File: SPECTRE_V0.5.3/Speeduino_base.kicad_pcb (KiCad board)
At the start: 2 copper layers, 100 x 93 mm, 197 parts, among them J1 Conn_01x06_Male, J2 Conn_02x04_Odd_Even, J3 ProtoArea, Q1 AO3400, Q10 BSP78, Q11 BSP78, Q12 AO3400, Q13 BSP78, Q14 BSP78, Q15 BSP78, Q16 BSP78, Q17 BSP78, Q18 BSP78, Q19 BSP78, Q20 BSP78, Q21 BSP78, Q6 AO3400, Q7 AO3400, U1 MAX9926UAEE+, U10 MIC4427, U2 LM78M05_TO220, U3 TL431DBZ, U4 molex_48pin, U5 TJA1050, U6 MAX3232, U7 MIC4427, U8 MIC4427, U9 MIC4427

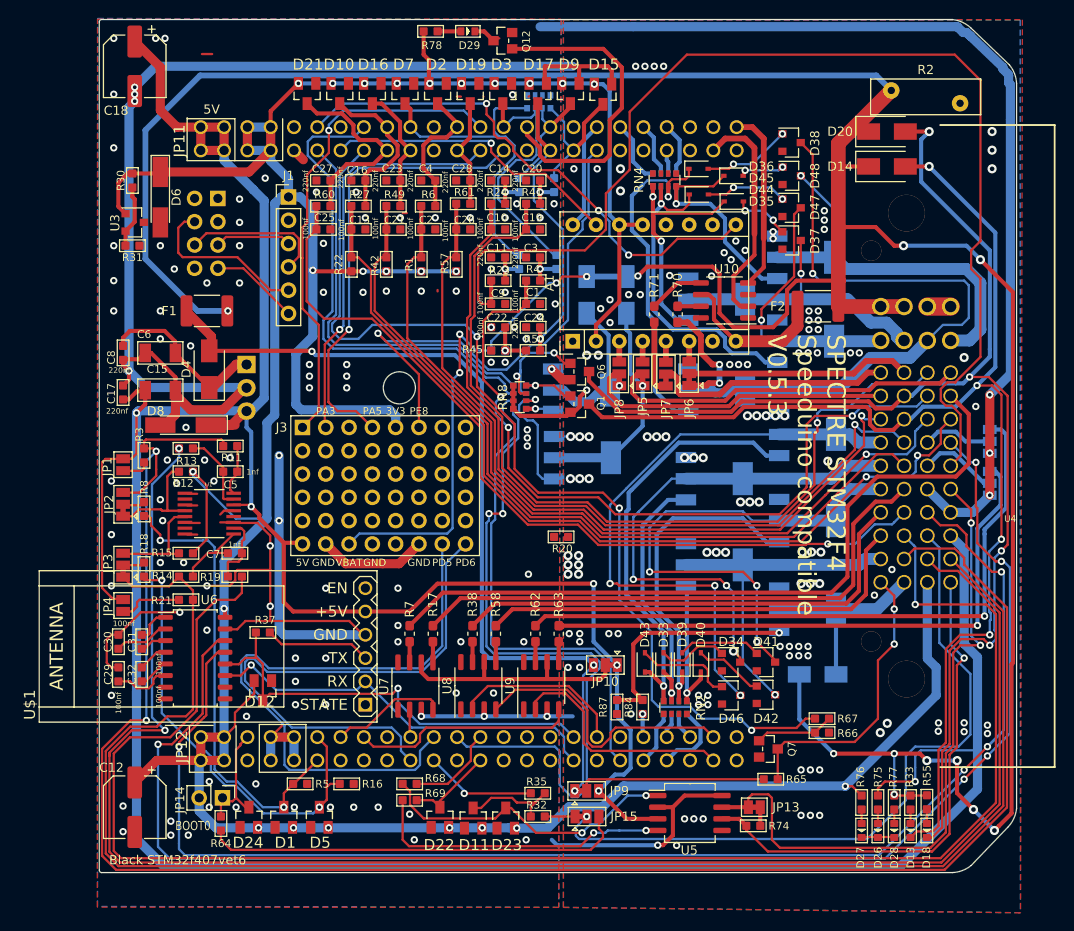
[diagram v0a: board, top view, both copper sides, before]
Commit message: Increased VBAT width
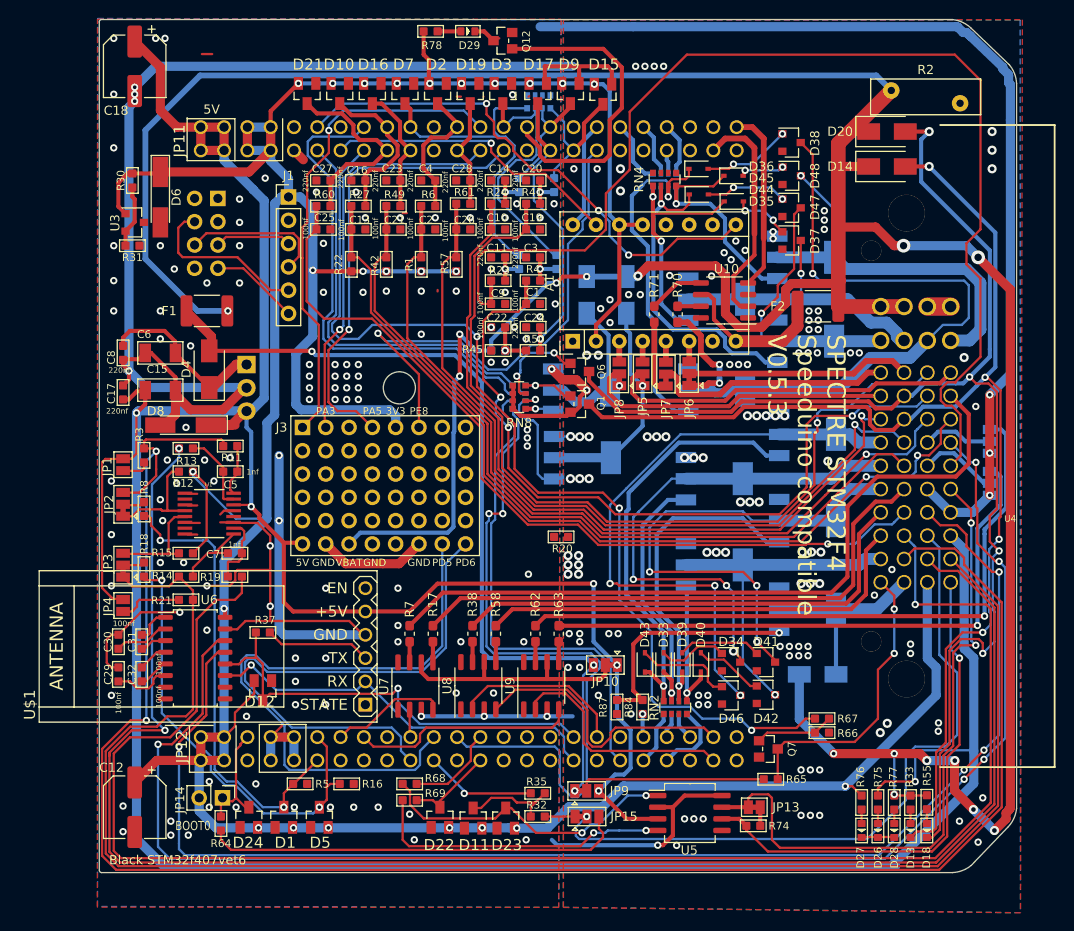
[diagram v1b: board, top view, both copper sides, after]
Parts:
- U4: footprint rusefi_lib:Molex_48 -> Speeduino_base:Molex_48
- moved RN4 0.07 mm to (165.2, 53.0)
- moved RN7 0.06 mm to (149.4, 76.7)
- moved RN8 0.06 mm to (149.4, 76.7)
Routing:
- net RS232_RX: track 150.8 -> 148.4 mm
- net PWR_GND: track 160.8 -> 163.0 mm, vias 129 -> 131
- net Net-(JP15-Pad2): track 77.0 -> 74.9 mm
- net FUEL_PUMP: track 136.1 -> 135.1 mm
- net FAN: track 139.9 -> 140.8 mm
- net VR2+: track 175.4 -> 174.5 mm
- net VR1+: track 204.8 -> 204.0 mm
- net VR1-: track 182.0 -> 181.2 mm
- net VR2-: track 176.3 -> 175.5 mm
- net CANH: track 73.0 -> 72.2 mm
- net VBAT: track 362.5 -> 361.8 mm
- net GND: vias 110 -> 121
